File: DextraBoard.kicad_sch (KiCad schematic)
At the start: 16 parts, among them J6 USB_C_Receptacle_USB2.0, J9 USB_C_Receptacle_USB2.0, SW1 SW_SPDT, SW2 SW_SPDT, U1 CH340C, U2 ESP32-WROOM-32D, U7 MCP73811T-420I-OT

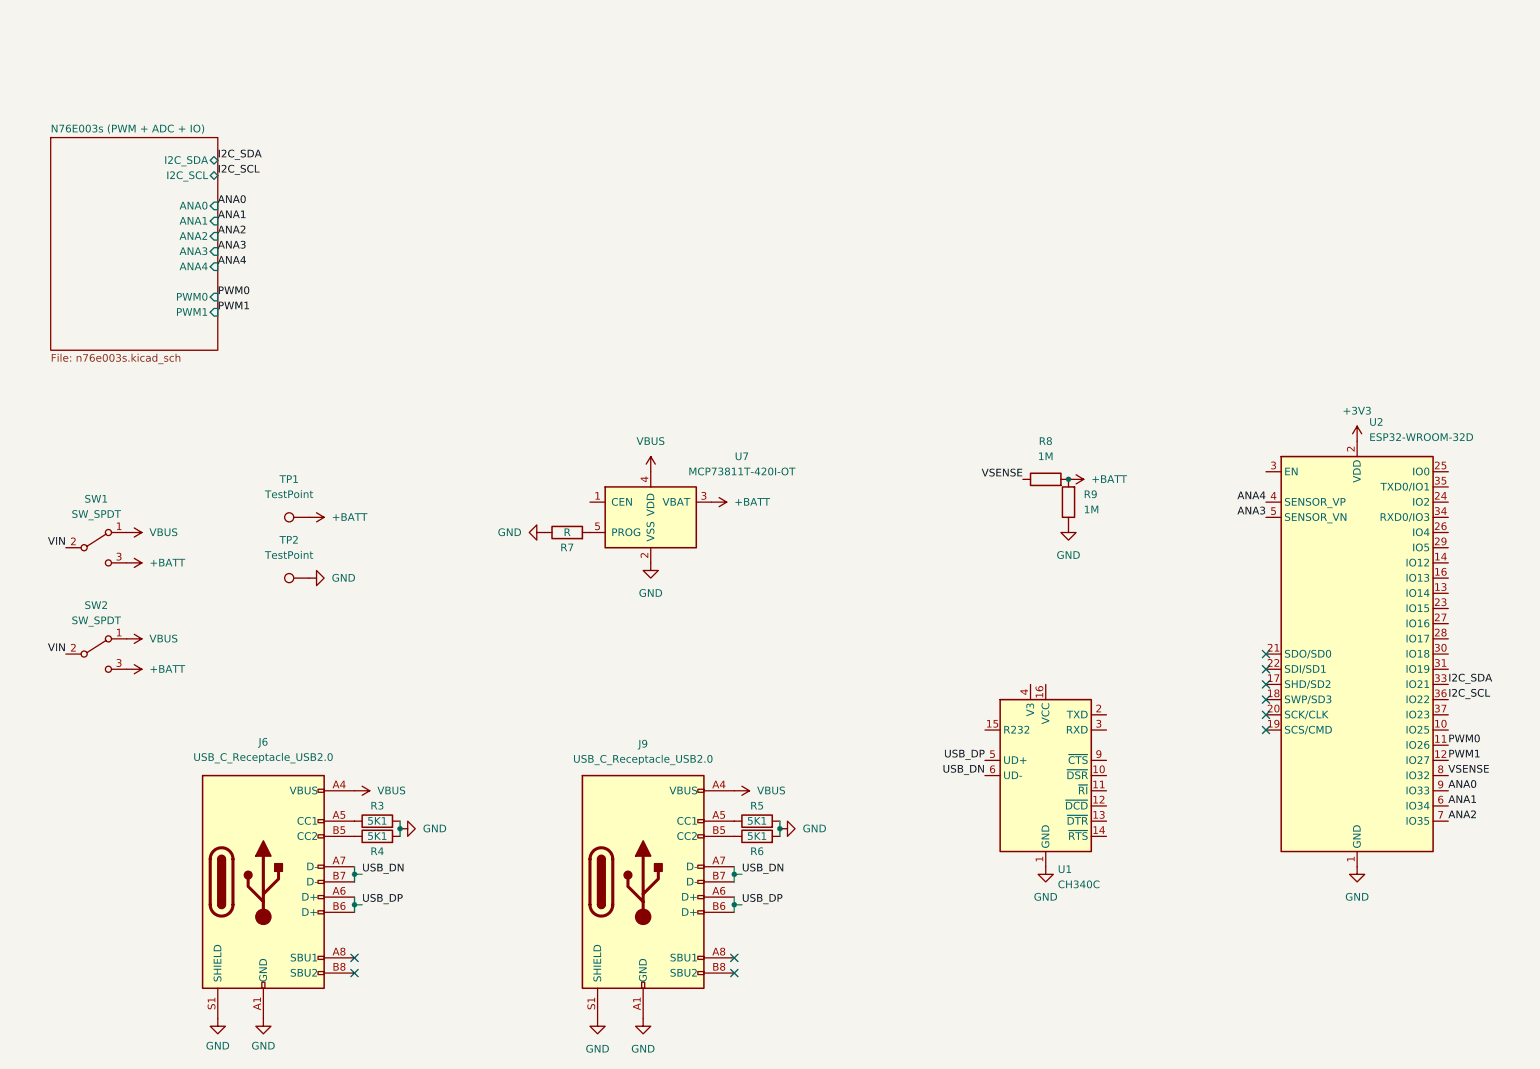
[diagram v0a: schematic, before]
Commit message: replaced esp32wroom by esp32 pico d4 and moved all component on one side
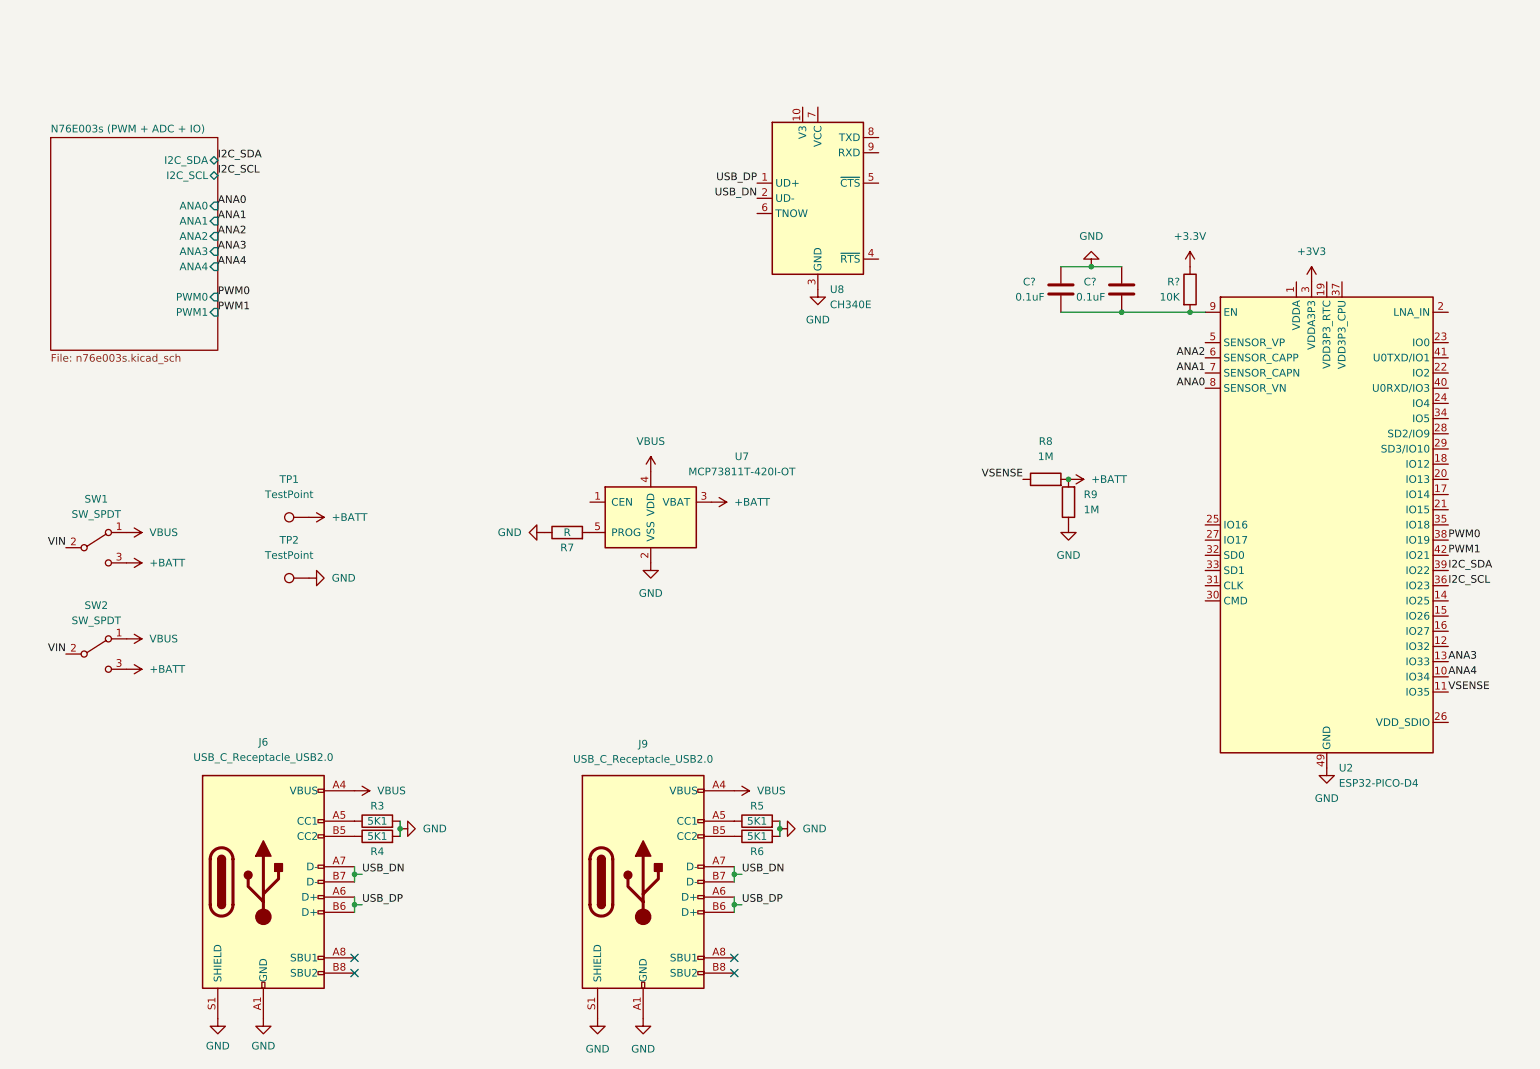
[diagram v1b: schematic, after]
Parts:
- removed U1: CH340C, Package_SO:SOIC-16_3.9x9.9mm_P1.27mm, symbol Interface_USB:CH340C
- removed U2: ESP32-WROOM-32D, RF_Module:ESP32-WROOM-32, symbol RF_Module:ESP32-WROOM-32D
- added C? (x2): 0.1uF, symbol Device:C
- added R?: 10K, symbol Device:R
- added U2: ESP32-PICO-D4, Package_DFN_QFN:QFN-48-1EP_7x7mm_P0.5mm_EP5.3x5.3mm, symbol RF_Module:ESP32-PICO-D4
- added U8: CH340E, Package_SO:MSOP-10_3x3mm_P0.5mm, symbol Interface_USB:CH340E
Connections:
- net +3V3: now also R?.1, U2.3 (VDDA3P3), U2.4 (VDDA3P3)
- net ANA0: now also U2.8 (SENSOR_VN)
- net ANA1: now also U2.7 (SENSOR_CAPN)
- net ANA2: now also U2.6 (SENSOR_CAPP)
- net ANA3: now also U2.13 (IO33)
- net ANA4: now also U2.10 (IO34)
- net GND: now also C?.1, C?.1, U2.49 (GND), U8.3 (GND)
- net I2C_SCL: now also U2.36 (IO23)
- net I2C_SDA: now also U2.39 (IO22)
- net PWM0: now also U2.38 (IO19)
- net PWM1: now also U2.42 (IO21)
- net USB_DN: now also U8.2 (UD-)
- net USB_DP: now also U8.1 (UD+)
- net VSENSE: now also U2.11 (IO35)
- new net: C?.2, C?.2, R?.2, U2.9 (EN)
- new net: U2.1 (VDDA), U2.43 (VDDA), U2.46 (VDDA)
- no-connect marks 10 -> 4

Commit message: redesigned everything x)
new BMS design, switched to ESP32-S3 with external antenna, implement USB-C PD, add analog mux, add PWM controller, add USB to serial
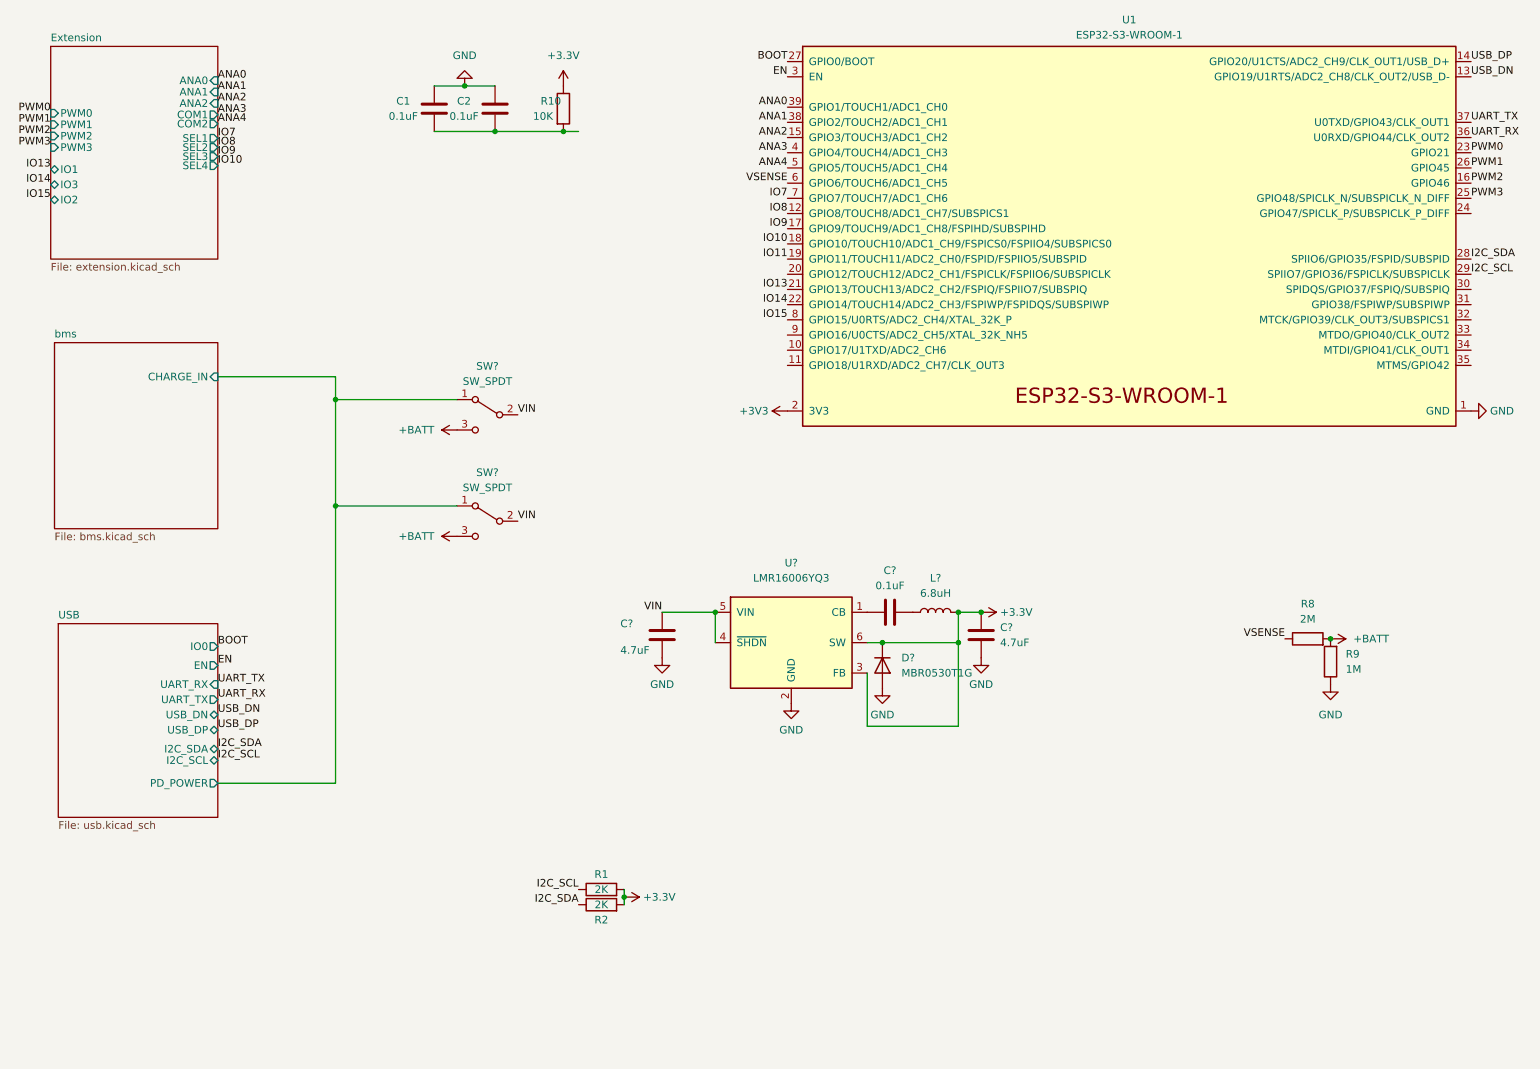
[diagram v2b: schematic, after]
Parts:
- removed J6, J9: USB_C_Receptacle_USB2.0, Connector_USB:USB_C_Receptacle_GCT_USB4085, symbol Connector:USB_C_Receptacle_USB2.0
- removed R3, R4, R5, R6: 5K1, Resistor_SMD:R_0201_0603Metric, symbol Device:R
- removed R7: R, Resistor_SMD:R_0201_0603Metric, symbol Device:R
- removed SW1, SW2: SW_SPDT, Button_Switch_THT:SW_CuK_OS102011MA1QN1_SPDT_Angled, symbol Switch:SW_SPDT
- removed TP1, TP2: TestPoint, TestPoint:TestPoint_Pad_D1.5mm, symbol Connector:TestPoint
- removed U2: ESP32-PICO-D4, Package_DFN_QFN:QFN-48-1EP_7x7mm_P0.5mm_EP5.3x5.3mm, symbol RF_Module:ESP32-PICO-D4
- removed U7: MCP73811T-420I-OT, Package_TO_SOT_SMD:SOT-23-5, symbol Battery_Management:MCP73811T-420I-OT
- removed U8: CH340E, Package_SO:MSOP-10_3x3mm_P0.5mm, symbol Interface_USB:CH340E
- added C?: 0.1uF, symbol Device:C
- added C? (x2): 4.7uF, symbol Device:C
- added D?: MBR0530T1G, symbol Device:D
- added L?: 6.8uH, symbol Device:L
- added R1, R2: 2K, Resistor_SMD:R_0402_1005Metric, symbol Device:R
- added SW? (x2): SW_SPDT, Button_Switch_THT:SW_CuK_OS102011MA1QN1_SPDT_Angled, symbol Switch:SW_SPDT
- added U1: ESP32-S3-WROOM-1, Espressif:ESP32-S3-WROOM-1U, symbol Espressif:ESP32-S3-WROOM-1
- added U?: LMR16006YQ3, Package_TO_SOT_SMD:SOT-23-6, symbol Regulator_Switching:LMR16006YQ3
- C1, C2: renamed from C?; footprint (none) -> Capacitor_SMD:C_0402_1005Metric
- R10: renamed from R?; footprint (none) -> Resistor_SMD:R_0402_1005Metric
- R8: value 1M -> 2M; footprint Resistor_SMD:R_0201_0603Metric -> Resistor_SMD:R_0402_1005Metric
- R9: footprint Resistor_SMD:R_0201_0603Metric -> Resistor_SMD:R_0402_1005Metric
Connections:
- net +3V3: now also U1.2 (3V3)
- net +BATT: now also SW?.3 (C), SW?.3 (C)
- net ANA0: now also U1.39 (GPIO1/TOUCH1/ADC1_CH0)
- net ANA1: now also U1.38 (GPIO2/TOUCH2/ADC1_CH1)
- net ANA2: now also U1.15 (GPIO3/TOUCH3/ADC1_CH2)
- net ANA3: now also U1.4 (GPIO4/TOUCH4/ADC1_CH3)
- net ANA4: now also U1.5 (GPIO5/TOUCH5/ADC1_CH4)
- net GND: now also C?.2, C?.2, D?.2 (A), U1.1 (GND), U1.40 (GND), U1.41 (GND), U?.2 (GND)
- net I2C_SCL: now also R1.1, U1.29 (SPIIO7/GPIO36/FSPICLK/SUBSPICLK)
- net I2C_SDA: now also R2.1, U1.28 (SPIIO6/GPIO35/FSPID/SUBSPID)
- net PWM0: now also U1.23 (GPIO21)
- net PWM1: now also U1.26 (GPIO45)
- net USB_DN: now also U1.13 (GPIO19/U1RTS/ADC2_CH8/CLK_OUT2/USB_D-)
- net USB_DP: now also U1.14 (GPIO20/U1CTS/ADC2_CH9/CLK_OUT1/USB_D+)
- net VIN: now also C?.1, SW?.2 (B), SW?.2 (B), U?.4 (~{SHDN}), U?.5 (VIN)
- net VSENSE: now also U1.6 (GPIO6/TOUCH6/ADC1_CH5)
- new net: C?.1, U?.1 (CB)
- new net: C?.2, L?.1
- new net +3.3V: C?.1, D?.1 (K), L?.2, R1.2, R2.2, U?.3 (FB), U?.6 (SW)
- new net BOOT: U1.27 (GPIO0/BOOT)
- new net EN: U1.3 (EN)
- new net IO10: U1.18 (GPIO10/TOUCH10/ADC1_CH9/FSPICS0/FSPIIO4/SUBSPICS0)
- new net IO11: U1.19 (GPIO11/TOUCH11/ADC2_CH0/FSPID/FSPIIO5/SUBSPID)
- new net IO13: U1.21 (GPIO13/TOUCH13/ADC2_CH2/FSPIQ/FSPIIO7/SUBSPIQ)
- new net IO14: U1.22 (GPIO14/TOUCH14/ADC2_CH3/FSPIWP/FSPIDQS/SUBSPIWP)
- new net IO15: U1.8 (GPIO15/U0RTS/ADC2_CH4/XTAL_32K_P)
- new net IO7: U1.7 (GPIO7/TOUCH7/ADC1_CH6)
- new net IO8: U1.12 (GPIO8/TOUCH8/ADC1_CH7/SUBSPICS1)
- new net IO9: U1.17 (GPIO9/TOUCH9/ADC1_CH8/FSPIHD/SUBSPIHD)
- new net PWM2: U1.16 (GPIO46)
- new net PWM3: U1.25 (GPIO48/SPICLK_N/SUBSPICLK_N_DIFF)
- new net UART_RX: U1.36 (U0RXD/GPIO44/CLK_OUT2)
- new net UART_TX: U1.37 (U0TXD/GPIO43/CLK_OUT1)
- new net USB/PD_POWER: SW?.1 (A), SW?.1 (A)
- no-connect marks 4 -> 0
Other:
- sheet N76E003s (PWM + ADC + IO) renamed Extension
- added sheet USB (usb.kicad_sch)
- added sheet bms (bms.kicad_sch)
- sheet Extension: file n76e003s.kicad_sch -> extension.kicad_sch
- sheet Extension ports: added COM1, COM2, IO1, IO2, IO3, PWM2, PWM3, SEL1, SEL2, SEL3, SEL4; removed ANA3, ANA4, I2C_SCL, I2C_SDA
- moved on the sheet: C1, C2, R10, R8, R9
